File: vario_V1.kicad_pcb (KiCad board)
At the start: 2 copper layers, 34 parts, among them J1 Conn_01x02_Male, J2 Conn_ARM_JTAG_SWD_10, J3 Conn_01x02_Male, Q1 MMBT3904, SW1 SW_DIP_x01, U1 TPS61221DCK, U2 STM32F042F6Px, U3 PCF8551ATT_AJ, U4 LPS25HB, U5 LCD-S401C52TR

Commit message: Basic layout done- passes DRC, not dense, no power plane
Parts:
- removed C10, C8: 100nF, Capacitor_SMD:C_0402_1005Metric
- removed U3: PCF8551ATT_AJ, lcd:SOP50P810X120-48N
- removed U5: LCD-S401C52TR, vario:DIP-40_W32.4mm_Socket
- BT1: moved to B.Cu
- moved BZ1 211.2 mm to (44.9, 145.6), turned to 90 degrees
- moved R5 210.9 mm to (40.0, 150.7), turned to 90 degrees
- moved R6 203.9 mm to (44.0, 153.7), turned to 90 degrees
- moved Q1 200.7 mm to (49.6, 151.3), turned to 90 degrees
- moved J1 158.2 mm to (35.6, 168.4)
- moved J2 156.3 mm to (39.4, 171.1), turned to 90 degrees
- moved J3 154.3 mm to (49.0, 170.9), turned to 180 degrees
- moved R2 153.5 mm to (52.3, 169.7)
- moved C9 150.9 mm to (56.8, 157.4)
- moved U4 150.9 mm to (56.8, 159.7)
- moved C4 142.2 mm to (33.8, 162.4), turned to 90 degrees
- moved C3 141.4 mm to (35.2, 162.4), turned to 90 degrees
- moved C2 139.4 mm to (36.9, 161.9), turned to 90 degrees
- moved U2 138.0 mm to (42.1, 162.3), turned to 180 degrees
- moved C7 134.8 mm to (47.1, 161.5), turned to 90 degrees
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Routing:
- net /COM: track 110.2 -> 0.00 mm
- net +3V3: track 18.0 -> 126.1 mm
- net /4A: track 34.0 -> 0.00 mm, vias 1 -> 0
- net /4B: track 29.0 -> 0.00 mm, vias 1 -> 0
- net /4F: track 28.9 -> 0.00 mm, vias 1 -> 0
- net /3B: track 26.2 -> 0.00 mm, vias 1 -> 0
- net /4C: track 25.7 -> 0.00 mm, vias 1 -> 0
- net /3A: track 25.1 -> 0.00 mm, vias 1 -> 0
- net /1E: track 24.8 -> 0.00 mm
- net /4G: track 24.3 -> 0.00 mm, vias 1 -> 0
- net /1D: track 24.0 -> 0.00 mm
- net /3F: track 23.6 -> 0.00 mm, vias 2 -> 0
- net /4D: track 23.5 -> 0.00 mm, vias 1 -> 0
- net /1C: track 23.1 -> 0.00 mm
- net Net-(BZ1-Pad2): track 0.00 -> 22.9 mm
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- added copper zone on B.Cu, net GND
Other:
- board outline added: 55.1 x 39.9 mm

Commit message: Added power plane
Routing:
- net +3V3: track 126.1 -> 108.4 mm
- added copper zone on F.Cu, net +3V3
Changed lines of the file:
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@@
     (thickness 1.6)
     (drawings 8)
-    (tracks 186)
+    (tracks 182)
     (zones 0)
     (modules 30)
@@
   (segment (start 46.905 162.6564) (end 44.9249 162.6564) (width 0.2032) (layer F.Cu) (net 3))
   (segment (start 47.1424 162.419) (end 46.905 162.6564) (width 0.2032) (layer F.Cu) (net 3))
-  (segment (start 44.8564 146.7472) (end 40.0304 151.5732) (width 0.2032) (layer F.Cu) (net 3))
   (segment (start 44.8564 145.5928) (end 44.8564 146.7472) (width 0.2032) (layer F.Cu) (net 3))
   (segment (start 60.398 164.589) (end 54.898 164.589) (width 0.2032) (layer F.Cu) (net 3))
@@
   (segment (start 38.20839 161.42161) (end 36.8808 162.7492) (width 0.2032) (layer F.Cu) (net 3))
   (segment (start 38.20839 153.39521) (end 38.20839 161.42161) (width 0.2032) (layer F.Cu) (net 3))
-  (segment (start 40.0304 151.5732) (end 38.20839 153.39521) (width 0.2032) (layer F.Cu) (net 3))
   (segment (start 47.932491 162.1306) (end 48.9482 162.1306) (width 0.2032) (layer F.Cu) (net 3))
-  (segment (start 34.455999 166.812153) (end 38.415762 162.85239) (width 0.2032) (layer F.Cu) (net 3))
   (segment (start 34.455999 171.471921) (end 34.455999 166.812153) (width 0.2032) (layer F.Cu) (net 3))
   (segment (start 47.210701 162.85239) (end 47.932491 162.1306) (width 0.2032) (layer F.Cu) (net 3))
@@
   (segment (start 53.9226 159.4374) (end 51.2294 162.1306) (width 0.2032) (layer F.Cu) (net 3))
   (segment (start 38.415762 162.85239) (end 47.210701 162.85239) (width 0.2032) (layer F.Cu) (net 3))
-  (segment (start 41.797 164.516) (end 39.9374 162.6564) (width 0.2032) (layer F.Cu) (net 3))
   (segment (start 39.9374 162.6564) (end 39.1999 162.6564) (width 0.2032) (layer F.Cu) (net 3))
   (segment (start 41.797 167.132) (end 41.797 164.516) (width 0.2032) (layer F.Cu) (net 3))
@@
     (connect_pads (clearance 0.508))
     (min_thickness 0.254)
+    (fill yes (arc_segments 32) (thermal_gap 0.508) (thermal_bridge_width 0.508))
+    (polygon
+      (pts
+        (xy 71.882 151.638) (xy 71.882 173.99) (xy 17.78 173.99) (xy 17.78 151.638) (xy 35.814 135.128)
+        (xy 55.626 135.128)
+      )
+    )
+  )
+  (zone (net 3) (net_name +3V3) (layer F.Cu) (hatch edge 0.508)
+    (connect_pads (clearance 0.508))
+    (min_thickness 0.254)

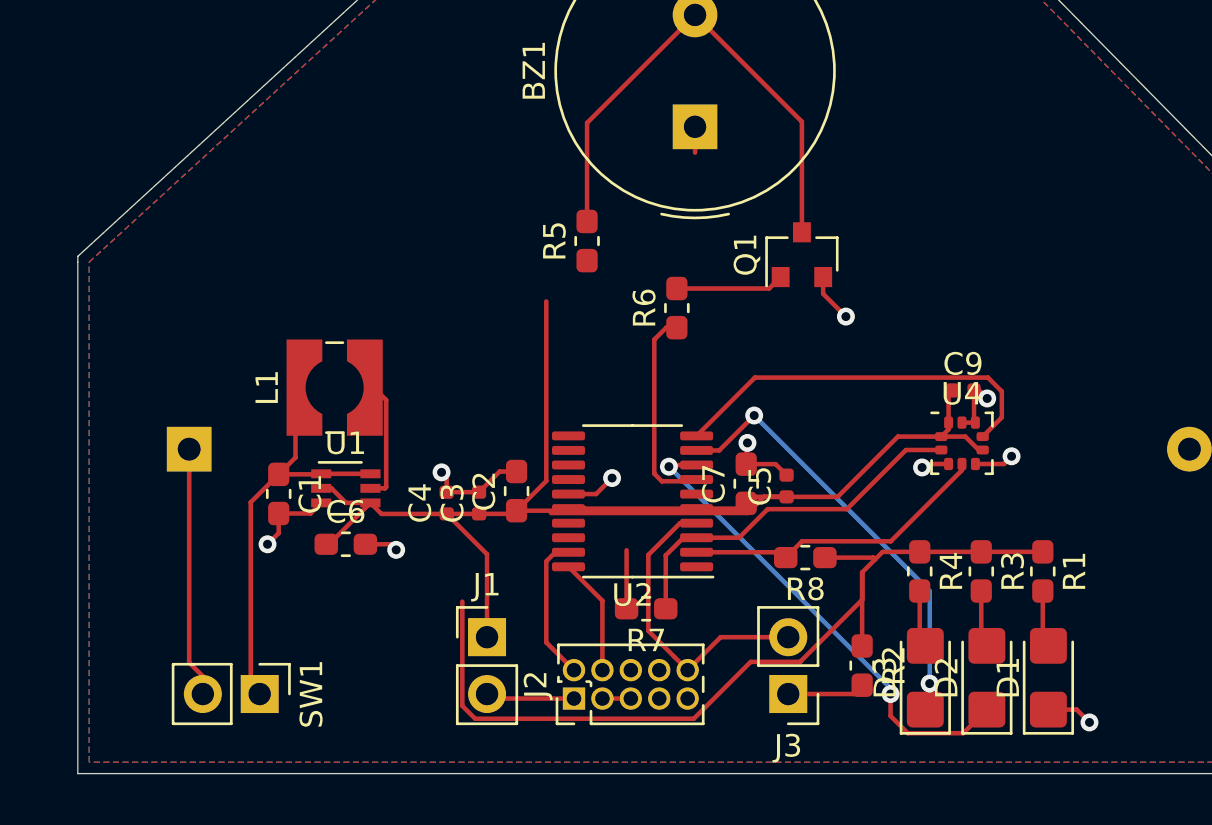
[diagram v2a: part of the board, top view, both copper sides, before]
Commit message: Silkscreen: fixed designator, added text
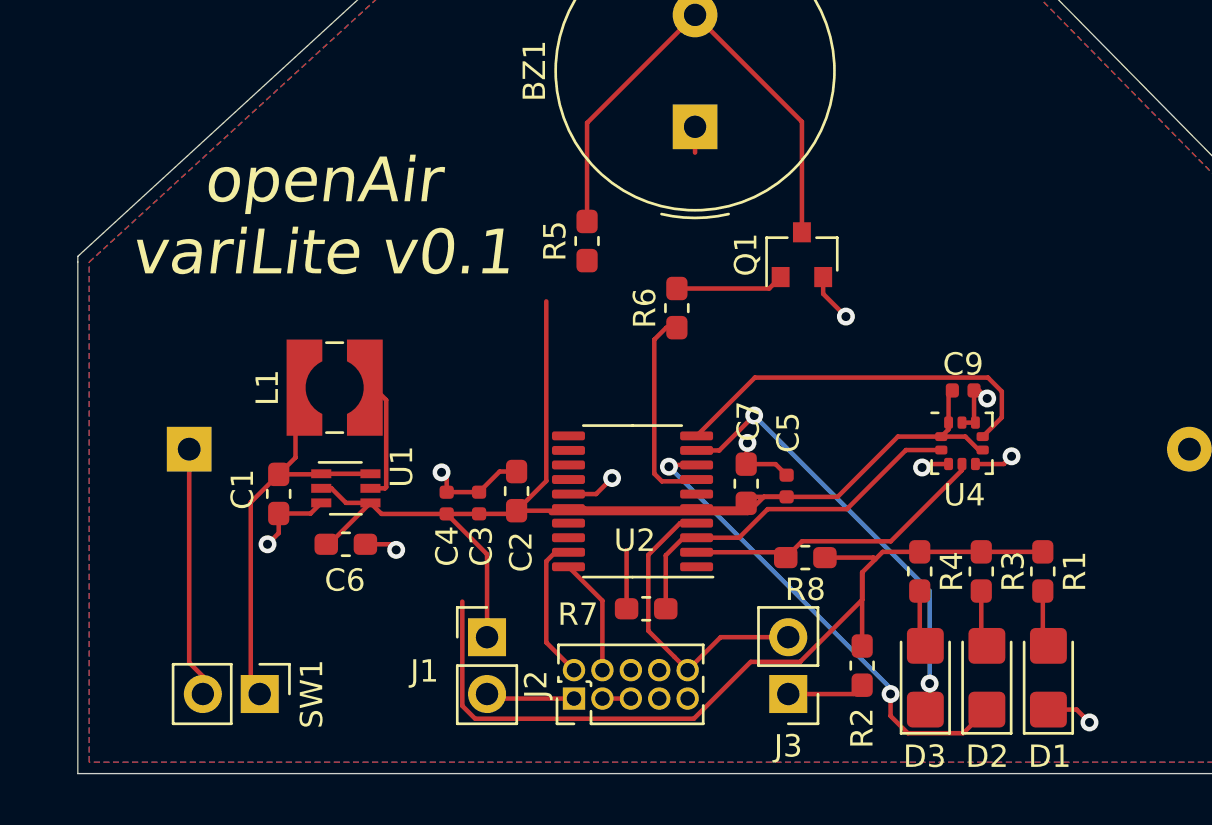
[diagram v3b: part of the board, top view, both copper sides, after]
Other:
- board text added: "openAir variLite v0.1"
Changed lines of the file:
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@@
   (general
     (thickness 1.6)
-    (drawings 8)
+    (drawings 9)
     (tracks 182)
     (zones 0)
@@
   (page A4)
   (layers
-    (0 F.Cu signal)
-    (31 B.Cu signal)
+    (0 F.Cu signal hide)
+    (31 B.Cu signal hide)
     (32 B.Adhes user)
     (33 F.Adhes user)
@@
     (tags "capacitor handsolder")
     (attr smd)
-    (fp_text reference C1 (at 0 -1.43 90) (layer F.SilkS)
+    (fp_text reference C1 (at -0.202 1.612 90) (layer F.SilkS)
       (effects (font (size 1 1) (thickness 0.15)))
     )
@@
     (tags "capacitor handsolder")
     (attr smd)
-    (fp_text reference C2 (at 0 -1.43 90) (layer F.SilkS)
+    (fp_text reference C2 (at -2.7178 0.2032 90) (layer F.SilkS)
       (effects (font (size 1 1) (thickness 0.15)))
     )
@@
     (tags capacitor)
     (attr smd)
-    (fp_text reference C3 (at 0 -1.17 90) (layer F.SilkS)
+    (fp_text reference C3 (at -1.9328 0.1016 90) (layer F.SilkS)
       (effects (font (size 1 1) (thickness 0.15)))
     )
@@
     (tags capacitor)
     (attr smd)
-    (fp_text reference C4 (at 0 -1.17 90) (layer F.SilkS)
+    (fp_text reference C4 (at -1.9304 0.0254 90) (layer F.SilkS)
       (effects (font (size 1 1) (thickness 0.15)))
     )
@@
     (tags capacitor)
     (attr smd)
-    (fp_text reference C5 (at 0 -1.17 90) (layer F.SilkS)
+    (fp_text reference C5 (at 2.3876 0.0738 90) (layer F.SilkS)
       (effects (font (size 1 1) (thickness 0.15)))
     )
@@
     (tags "capacitor handsolder")
     (attr smd)
-    (fp_text reference C6 (at 0 -1.43) (layer F.SilkS)
+    (fp_text reference C6 (at -0.04 1.612) (layer F.SilkS)
       (effects (font (size 1 1) (thickness 0.15)))
     )
@@
     (tags "capacitor handsolder")
     (attr smd)
-    (fp_text reference C7 (at 0 -1.43 90) (layer F.SilkS)
+    (fp_text reference C7 (at 2.794 0.1016 90) (layer F.SilkS)
       (effects (font (size 1 1) (thickness 0.15)))
     )
@@
     (tags "LED castellated")
     (attr smd)
-    (fp_text reference D1 (at 0 -1.78 90) (layer F.SilkS)
+    (fp_text reference D1 (at -3.522 0.058 180) (layer F.SilkS)
       (effects (font (size 1 1) (thickness 0.15)))
     )
@@
     (tags "LED castellated")
     (attr smd)
-    (fp_text reference D2 (at 0 -1.78 90) (layer F.SilkS)
+    (fp_text reference D2 (at -3.522 0.014 180) (layer F.SilkS)
       (effects (font (size 1 1) (thickness 0.15)))
     )
@@
     (tags "LED castellated")
     (attr smd)
-    (fp_text reference D3 (at 0 -1.78 90) (layer F.SilkS)
+    (fp_text reference D3 (at -3.522 -0.03 180) (layer F.SilkS)
       (effects (font (size 1 1) (thickness 0.15)))
     )
@@
     (descr "Through hole straight pin header, 1x02, 2.54mm pitch, single row")
     (tags "Through hole pin header THT 1x02 2.54mm single row")
-    (fp_text reference J1 (at 0 -2.33) (layer F.SilkS)
+    (fp_text reference J1 (at -2.794 1.524) (layer F.SilkS)
       (effects (font (size 1 1) (thickness 0.15)))
     )
@@
     (tags "resistor handsolder")
     (attr smd)
-    (fp_text reference R2 (at 0 -1.43 90) (layer F.SilkS)
+    (fp_text reference R2 (at 2.794 0 270) (layer F.SilkS)
       (effects (font (size 1 1) (thickness 0.15)))
     )
@@
     (tags "resistor handsolder")
     (attr smd)
-    (fp_text reference R7 (at 0 -1.43) (layer F.SilkS)
+    (fp_text reference R7 (at 3.048 -0.254) (layer F.SilkS)
       (effects (font (size 1 1) (thickness 0.15)))
     )
@@
     (tags "R-PDSO-G6 SC-70-6")
     (attr smd)
-    (fp_text reference U1 (at 0 -2) (layer F.SilkS)
+    (fp_text reference U1 (at 2.5 -0.968 90) (layer F.SilkS)
       (effects (font (size 1 1) (thickness 0.15)))
     )
@@
     (tags "TSSOP SO")
     (attr smd)
-    (fp_text reference U2 (at 0 -4.2) (layer F.SilkS)
+    (fp_text reference U2 (at -0.1016 -1.7526) (layer F.SilkS)
       (effects (font (size 1 1) (thickness 0.15)))
     )
@@
     (tags "ST HLGA NoLead")
     (attr smd)
-    (fp_text reference U4 (at 0 -2.2) (layer F.SilkS)
+    (fp_text reference U4 (at 0.1102 2.3146) (layer F.SilkS)
       (effects (font (size 1 1) (thickness 0.15)))
     )
@@
     )
   )
+  (gr_text "openAir\nvariLite v0.1" (at 28.194 149.606) (layer F.SilkS)
+    (effects (font (size 2 2) (thickness 0.15) italic))
+  )
   (gr_line (start 55.88 134.62) (end 72.39 151.384) (layer Edge.Cuts) (width 0.05))

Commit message: Finishing layout
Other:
- board text added: "variLite v0.1"
- board text removed: "openAir variLite v0.1"
